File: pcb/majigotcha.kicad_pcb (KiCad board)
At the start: 2 copper layers, 59.7 x 40.5 mm, 12 parts, among them SW1 SW_Push, SW2 SW_Push, SW3 SW_Push, U2 DM-OLED096-636, U3 TPP233-capacitive, U4 TOUCH CAPACITIVE, U5 XIAO-ESP32-S3-SMD

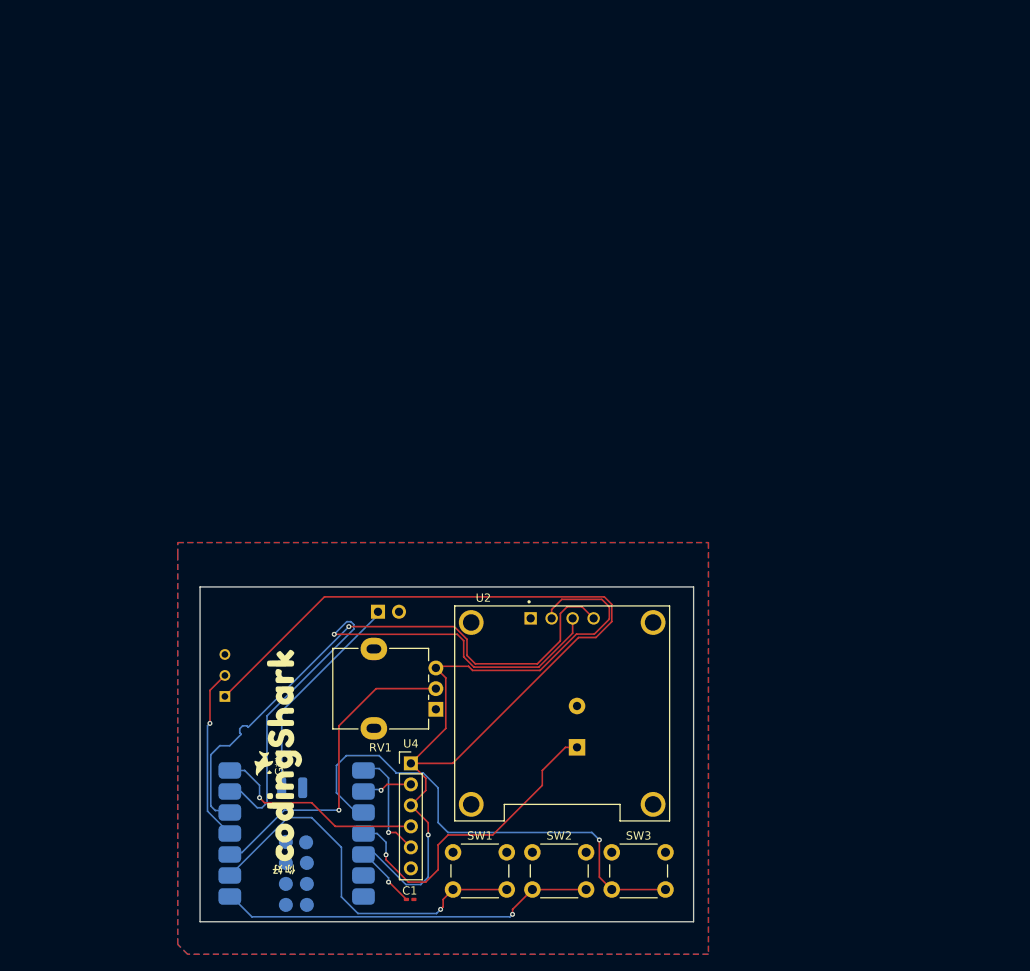
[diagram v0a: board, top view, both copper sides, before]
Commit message: add firmware! oh and change of pcb wiring
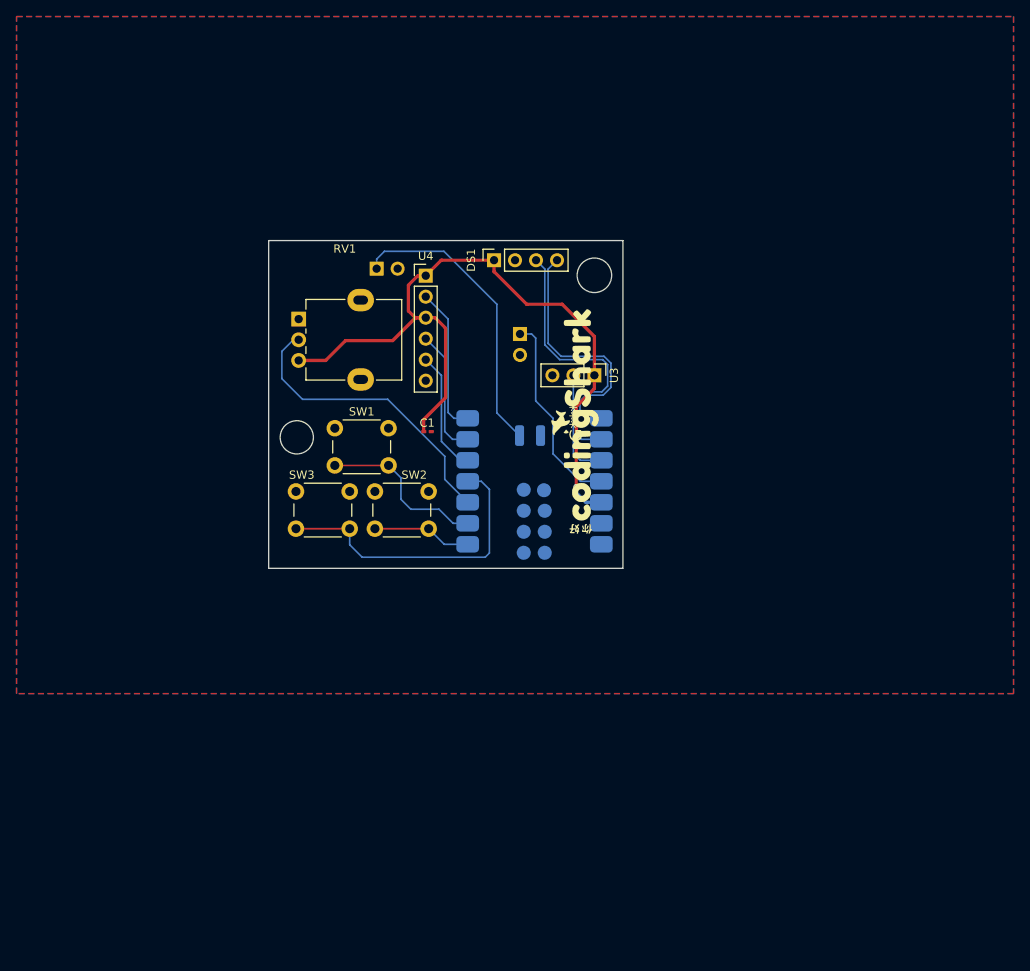
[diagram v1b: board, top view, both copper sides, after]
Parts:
- removed U2: DM-OLED096-636, DM-OLED096-636:MODULE_DM-OLED096-636
- added DS1: OLED_128X64_1.3_I2C, Connector_PinSocket_2.54mm:PinSocket_1x04_P2.54mm_Vertical, F.Cu at (181.7, 71.2)
- BUZZER1: footprint Buzzer_Beeper:Buzzer_TDK_PS1240P02BT_D12.2mm_H6.5mm -> Connector_PinSocket_2.54mm:PinSocket_1x02_P2.54mm_Vertical
- U3: footprint DFR0299:TTP223-CAPACITIVE -> Connector_PinHeader_2.54mm:PinHeader_1x03_P2.54mm_Vertical; moved to F.Cu
- moved U4 59.0 mm to (173.4, 73.0)
- moved SW3 58.0 mm to (157.7, 99.1)
- moved C1 56.6 mm to (173.6, 91.9)
- moved G*** 54.6 mm to (191.6, 90.8)
- moved SW1 53.3 mm to (162.4, 91.5)
- moved U5 51.4 mm to (186.8, 97.9)
- moved BUZZER1 50.5 mm to (184.8, 80.1), turned to 180 degrees
- moved RV1 50.0 mm to (158.0, 78.3), turned to 0 degrees
- moved SW2 47.6 mm to (167.2, 99.2)
- moved U3 47.6 mm to (193.8, 85.1), turned to -90 degrees
- moved BT1 41.5 mm to (167.5, 72.2)
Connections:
- U5 pad 10: BTN3 -> TOUCH
- U5 pad 4: TOUCH -> BTN3
- U5 pad 5: SDA -> RX
- U5 pad 6: SCL -> TX
- U5 pad 7: TX -> TOUCH_OUT
- U5 pad 8: RX -> SDA
- U5 pad 9: TOUCH_OUT -> SCK
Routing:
- net +3V3: track 167.5 -> 91.3 mm, vias 2 -> 1
- net SCL: track 69.7 -> 0.00 mm, vias 1 -> 0
- net SDA: track 70.6 -> 30.7 mm, vias 1 -> 0
- net BTN2: track 46.0 -> 12.0 mm, vias 1 -> 0
- net SCK: track 0.00 -> 33.7 mm
- net BTN1: track 46.4 -> 20.5 mm, vias 1 -> 0
- net BTN3: track 59.6 -> 36.9 mm, vias 1 -> 0
- net BUZ: track 39.1 -> 24.2 mm, vias 1 -> 0
- net TOUCH_OUT: track 6.09 -> 17.8 mm, vias 1 -> 0
- net TX: track 26.0 -> 15.3 mm, vias 1 -> 0
- net +BATT: track 26.1 -> 35.8 mm
- net TOUCH: track 21.1 -> 13.2 mm, vias 1 -> 0
- net POTENTIO: track 39.1 -> 36.2 mm, vias 1 -> 0
- net RX: track 13.6 -> 15.9 mm, vias 1 -> 0
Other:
- board size 59.7 x 40.5 mm -> 42.8 x 39.6 mm

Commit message: update gerbers
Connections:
- U5 pad 5: RX -> SDA
- U5 pad 6: TX -> SCK
- U5 pad 8: SDA -> TX
- U5 pad 9: SCK -> RX
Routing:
- net TX: track 15.3 -> 64.2 mm, vias 0 -> 1
- net RX: track 15.9 -> 63.4 mm, vias 0 -> 1
- net SDA: track 30.7 -> 49.2 mm
- net SCK: track 33.7 -> 46.1 mm
- net +BATT: track 35.8 -> 35.1 mm, vias 0 -> 1
- net GND: vias 0 -> 3
